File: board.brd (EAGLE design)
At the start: 160 x 100 mm, 109 parts, among them IC1 LMZ10501SILT, IC2 TPS61088RHLR, Q1 IRFML8244TRPBF, Q2 IRFML8244TRPBF, Q3 IRFML8244TRPBF, Q4 IRFML8244TRPBF, Q5 IRFML8244TRPBF, U1 TB6612FNG, U2 MPU6500, U3 STM32F405RG, X1 JST-XH

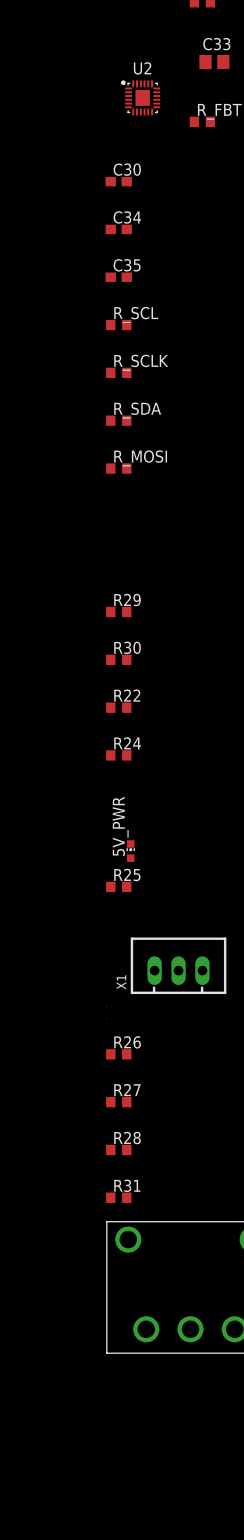
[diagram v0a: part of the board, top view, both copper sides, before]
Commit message: Changed IMU to bosch BMI088
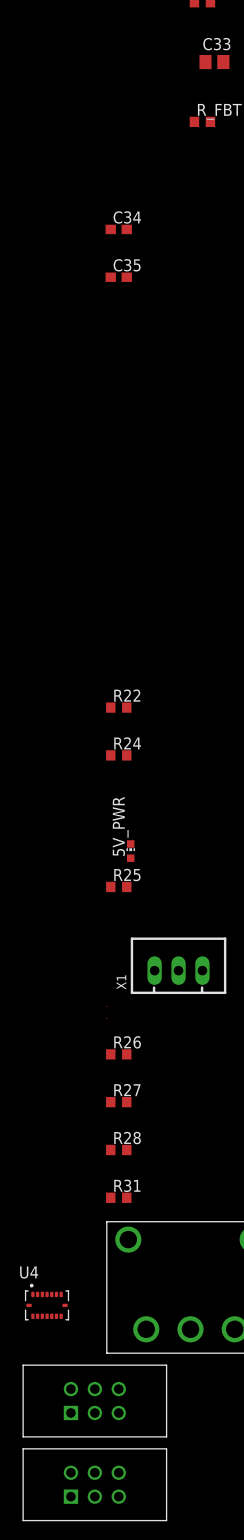
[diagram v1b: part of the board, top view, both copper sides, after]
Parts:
- removed C30: 0.1u, CASE-RCL:C0603
- removed R29, R30, R_MOSI, R_SCL, R_SCLK, R_SDA: 0, CASE-RCL:R0603
- removed U2: MPU6500, Isaks Bibliotek:QFN40P300X300X95-25T154X170
- added U$8, U$9: IE2-1024, Isaks Bibliotek:IE2-1024-ENCODER
- added U4: BMI088, Isaks Bibliotek:PQFN50P450X300X100-16N
- C34: value 10n -> 0.1u
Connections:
- removed net !CS: R30.1
- removed net INT: U2.12
- removed net MISO: U2.9
- removed net MOSI: R_MOSI.1
- removed net N$30: R_SCL.2, R_SCLK.2, U2.23
- removed net N$36: R29.2, R30.2, U2.22
- removed net SCLK: R_SCLK.1
- removed net VBAT: U3.1
- removed net VDDA: U3.13
- removed net VDD_1: U3.32
- removed net VDD_2: U3.48
- removed net VDD_3: U3.64
- removed net VDD_4: U3.19
- removed net VSSA: U3.12
- removed net VSS_1: U3.31
- removed net VSS_2: U3.47
- removed net VSS_3: U3.63
- removed net VSS_4: U3.18
- new net A0_ACCEL: U4.15
- new net A0_GYRO: U4.10
- new net INT1_ACC: U4.16
- new net INT1_GYRO: U4.12
- new net INT2_ACCEL: U4.1
- new net INT2_GYRO: U4.13
- net 3.3VA: now also U4.11, U4.14, U4.3, U4.7; no longer R29.1, U2.13, U2.8
- net GND_A: now also U4.4, U4.6; no longer C30.2, U2.11, U2.18, U2.20
- net N$28: now also U3.1, U3.10, U3.11, U3.12, U3.13, U3.14, U3.15, U3.16, U3.17, U3.18, U3.19, U3.2, U3.20, U3.21, U3.22, U3.23, U3.24, U3.25, U3.26, U3.27, U3.28, U3.29, U3.3, U3.30, U3.31, U3.32, U3.4, U3.5, U3.6, U3.7, U3.8, U3.9; no longer C30.1, U2.10
- net N$29: now also U3.33, U3.34, U3.35, U3.36, U3.37, U3.38, U3.39, U3.40, U3.41, U3.42, U3.43, U3.44, U3.45, U3.46, U3.47, U3.48, U3.49, U3.50, U3.51, U3.52, U3.53, U3.54, U3.55, U3.56, U3.57, U3.58, U3.59, U3.60, U3.61, U3.62, U3.63, U3.64; no longer R_MOSI.2, R_SDA.2, U2.24
- net SCL: now also U4.8; no longer R_SCL.1
- net SDA: now also U4.9; no longer R_SDA.1

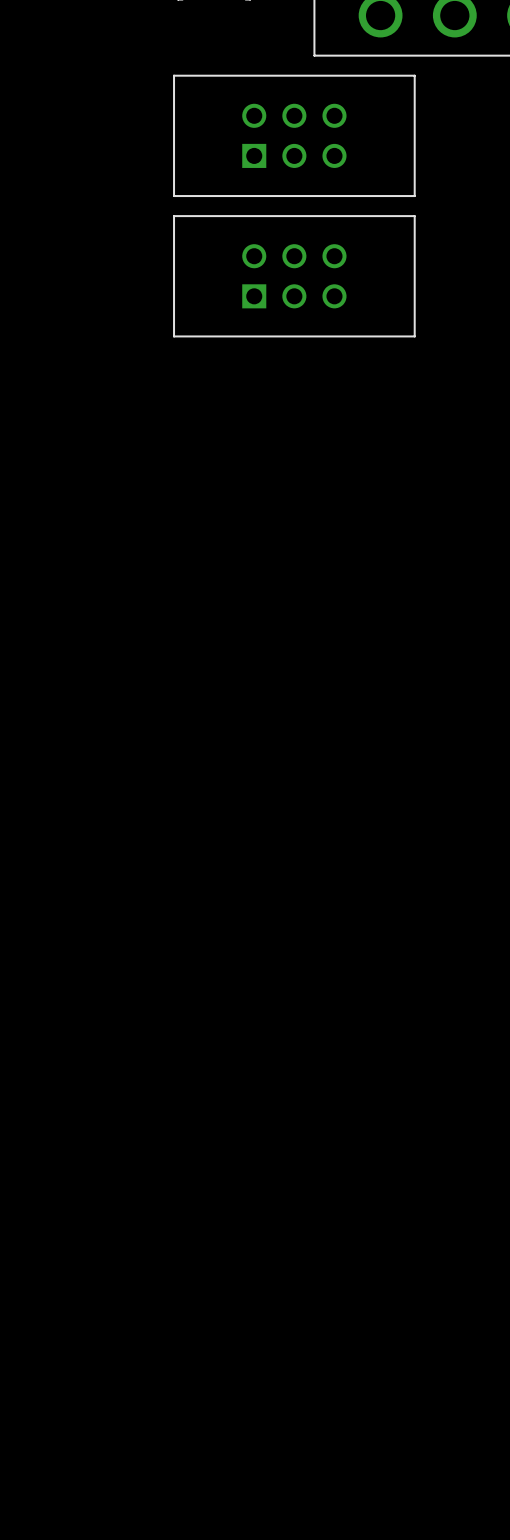
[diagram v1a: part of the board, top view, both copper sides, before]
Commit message: Pin Setup on MCU
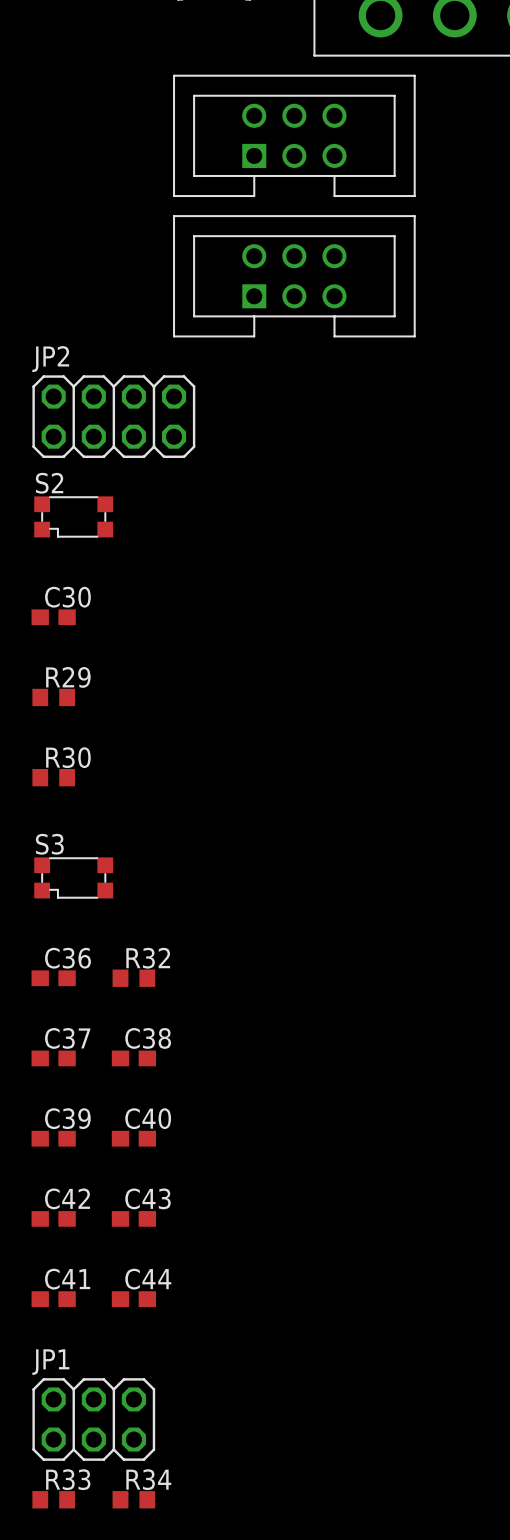
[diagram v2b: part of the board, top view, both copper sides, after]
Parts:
- added C30, C37, C38, C39, C40, C42, C43: 0.1u, CASE-RCL:C0603
- added C36, C44: 1u, CASE-RCL:C0603
- added C41: 10u, CASE-RCL:C0603
- added JP1: (no value), CASE-Pinhead:2X03
- added JP2: (no value), CASE-Pinhead:2X04
- added R29: 100k, CASE-RCL:R0603
- added R30, R32, R33, R34: 10k, CASE-RCL:R0603
- added S2, S3: KMR621NGLFS, CASE-Switches:KMR621NGLFS
- MOTOR_LEFT, MOTOR_RIGHT: value IE2-1024 -> IDC-6PIN
- renumbered U$8 to MOTOR_LEFT, U$9 to MOTOR_RIGHT
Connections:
- removed net A0_ACCEL: U4.15
- removed net A0_GYRO: U4.10
- removed net INT1_ACC: U4.16
- removed net INT1_GYRO: U4.12
- removed net INT2_ACCEL: U4.1
- removed net INT2_GYRO: U4.13
- removed net SCL: U4.8
- removed net SDA: U4.9
- removed net VOLM_BATT: R28.1, R31.2
- removed net VOLM_CELL1: R26.1, R27.2
- new net BOOT0: R34.2
- new net BOOT1: R33.1
- new net BUTTON_SEL: C30.1, R30.2, U3.28
- new net CS_ACCEL: U3.34, U4.14
- new net CS_GYRO: U3.33, U4.5
- new net ENC_L_A: MOTOR_RIGHT.6, U3.15
- new net ENC_L_B: MOTOR_RIGHT.5, U3.14
- new net ENC_R_A: MOTOR_LEFT.6, U3.21
- new net ENC_R_B: MOTOR_LEFT.5, U3.55
- new net INT_ACCEL: U3.24, U4.16
- new net INT_GYRO: U3.25, U4.12
- new net MISO: U3.35, U4.10, U4.15
- new net MOSI: U3.36, U4.9
- new net N$32: JP1.4, R33.2
- new net N$34: JP1.3, R34.1
- new net N$35: R29.2, R30.1, S2.1, S2.2
- new net RESET: C36.1, R32.1, S3.3, S3.4
- new net RX: JP2.5, U3.43
- new net SCK: U3.29, U4.8
- new net SWCLK: JP2.6, U3.49
- new net SWDIO: JP2.8, U3.46
- new net TX: JP2.7, U3.42
- new net VOLTM_BATT: R28.1, R31.2, U3.17
- new net VOLTM_CELL1: R26.1, R27.2, U3.20
- net 3.3V: now also C37.1, C38.1, C39.1, C40.1, C41.1, C42.1, C43.1, C44.1, JP1.1, JP1.2, JP2.1, JP2.2, R29.1, R32.2, U3.18, U3.31
- net 3.3VA: no longer U4.14, U4.7
- net 5V: now also MOTOR_LEFT.4, MOTOR_RIGHT.4
- net BUZZER: now also U3.44
- net FL_EMITTER: now also U3.23
- net FL_RECEIVER: now also U3.9
- net FR_EMITTER: now also U3.26
- net FR_RECEIVER: now also U3.10
- net GND: now also C30.2, C36.2, C37.2, C38.2, C39.2, C40.2, C41.2, C42.2, C43.2, C44.2, JP1.5, JP1.6, JP2.3, JP2.4, MOTOR_LEFT.3, MOTOR_RIGHT.3, S2.3, S2.4, S3.1, S3.2, U3.19, U3.32
- net GND_A: now also U4.7
- net LED_B: now also U3.50
- net LED_G: now also U3.51
- net LED_R: now also U3.52
- net L_EMITTER: now also U3.22
- net L_RECEIVER: now also U3.8
- net ML_IN1: now also U3.57
- net ML_IN2: now also U3.56
- net MOTOR_L_1: now also MOTOR_RIGHT.2
- net MOTOR_L_2: now also MOTOR_RIGHT.1
- net MOTOR_R_1: now also MOTOR_LEFT.2
- net MOTOR_R_2: now also MOTOR_LEFT.1
- net MR_IN1: now also U3.59
- net MR_IN2: now also U3.58
- net N$28: no longer U3.10, U3.11, U3.14, U3.15, U3.16, U3.17, U3.18, U3.19, U3.20, U3.21, U3.22, U3.23, U3.24, U3.25, U3.26, U3.27, U3.28, U3.29, U3.31, U3.32, U3.8, U3.9
- net N$29: no longer U3.33, U3.34, U3.35, U3.36, U3.42, U3.43, U3.44, U3.46, U3.49, U3.50, U3.51, U3.52, U3.55, U3.56, U3.57, U3.58, U3.59, U3.61, U3.62
- net PWM_L: now also U3.61
- net PWM_R: now also U3.62
- net R_EMITTER: now also U3.27
- net R_RECEIVER: now also U3.11
- net VOLTM_BOOST: now also U3.16

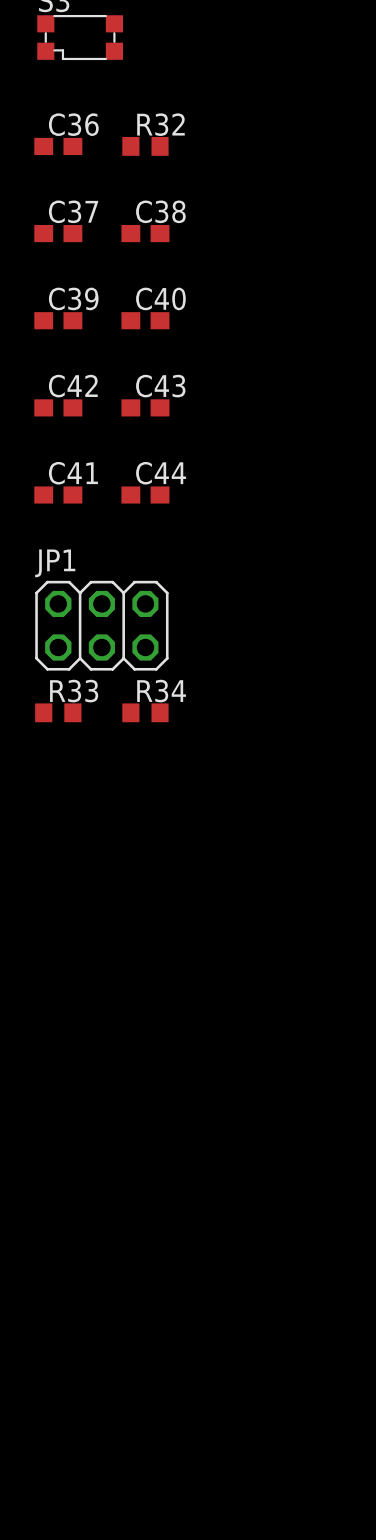
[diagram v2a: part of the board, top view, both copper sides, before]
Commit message: VSS + VDD
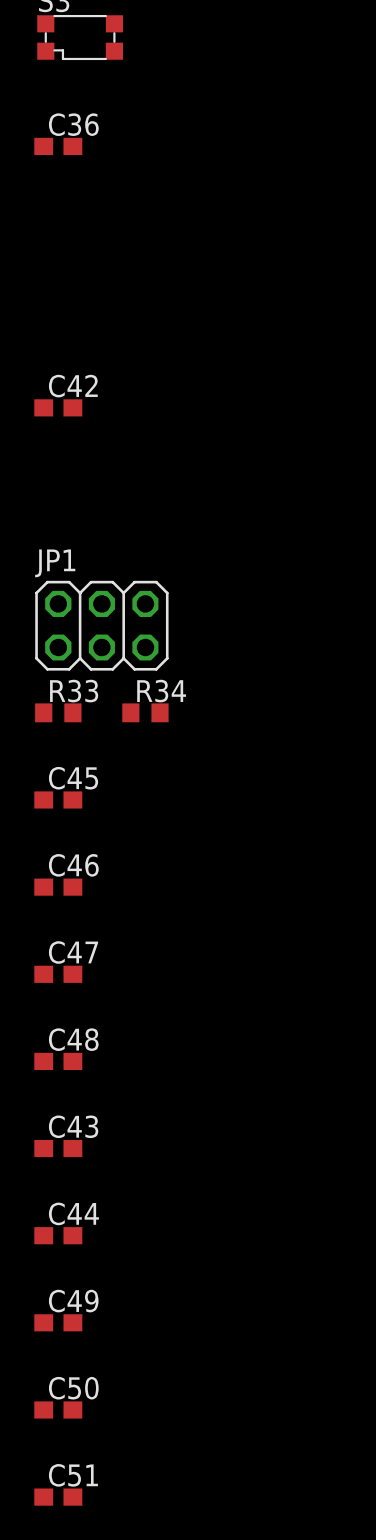
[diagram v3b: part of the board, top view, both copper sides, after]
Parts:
- removed C37, C38, C39, C40: 0.1u, CASE-RCL:C0603
- removed C41: 10u, CASE-RCL:C0603
- removed R32: 10k, CASE-RCL:R0603
- added C45, C46: 2.2u, CASE-RCL:C0603
- added C47, C48, C49, C50, C51: 0.1u, CASE-RCL:C0603
- C36: value 1u -> 0.1u
- C42: value 0.1u -> 10u
- moved C43 43.5 mm to (-260.4, -327.7)
- moved C44 43.5 mm to (-260.4, -332.7)
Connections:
- removed net BUTTON_SEL: C30.1, R30.2, U3.28
- new net BTN_SEL: C30.1, R30.2, U3.54
- new net N$30: C36.2, S3.1, S3.2
- new net N$36: C45.1, U3.31
- new net N$37: C46.1, U3.47
- net 3.3V: now also C47.1, C48.1, C49.1, C50.1, C51.1, U3.1, U3.19, U3.32, U3.48, U3.64; no longer C37.1, C38.1, C39.1, C40.1, C41.1, C43.1, C44.1, R32.2, U3.18, U3.31
- net 3.3VA: now also C43.1, C44.1, U3.13
- net BOOT0: now also U3.60
- net BOOT1: now also U3.28
- net GND: now also C45.2, C46.2, C47.2, C48.2, C49.2, C50.2, C51.2, U3.18, U3.63; no longer C36.2, C37.2, C38.2, C39.2, C40.2, C41.2, C43.2, C44.2, S3.1, S3.2, U3.19, U3.32
- net GND_A: now also C43.2, C44.2, U3.12
- net N$28: no longer U3.1, U3.12, U3.13, U3.7
- net N$29: no longer U3.47, U3.48, U3.54, U3.60, U3.63, U3.64
- net RESET: now also U3.7; no longer R32.1

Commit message: Oled + Hc05
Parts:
- added R32, R35, R36, R37: 10k, CASE-RCL:R0603
- added U$10: WIRELESS-BLUETOOTH-HC-05, diy-modules:WIRELESS-BLUETOOTH-HC-05
- added U$11: DISPLAY-OLED-128X64-I2C, diy-modules:DISPLAY-OLED-128X64-I2C
- moved JP2 445.5 mm to (64.8, 74.9)
- moved JP1 442.9 mm to (47.0, 24.1)
- moved MOTOR_RIGHT 394.7 mm to (62.2, 22.9)
- moved MOTOR_LEFT 357.0 mm to (20.3, 22.9)
- moved X1 333.4 mm to (35.6, 22.9)
- moved SW 329.4 mm to (12.7, 8.89), turned to 90 degrees
- moved D2 317.1 mm to (64.8, 90.2), turned to 330 degrees
- moved VR1 292.5 mm to (69.8, 14.0)
- moved C8 250.5 mm to (86.4, 91.4)
- moved R6 250.5 mm to (91.4, 91.4)
- moved C9 250.5 mm to (96.5, 91.4)
- moved Q1 250.5 mm to (76.2, 88.9)
- moved R8 250.5 mm to (101.6, 91.4)
- moved IC2 247.1 mm to (19.1, 14.0)
- moved D8 246.8 mm to (66.0, 92.7), turned to 330 degrees
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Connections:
- new net BT_RX: R32.2, U$10.3
- new net BT_TX: R36.2, U$10.2
- new net HEADER_RX: R35.2
- new net HEADER_TX: R37.2
- new net SCL: U$11.3
- new net SDA: U$11.4
- net 5V: now also U$10.5, U$11.2
- net GND: now also U$10.4, U$11.1
- net RX: now also R32.1, R35.1
- net TX: now also R36.1, R37.1
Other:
- board size 160 x 100 mm -> 80 x 100 mm
